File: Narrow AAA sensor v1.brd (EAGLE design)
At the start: 47 x 10.8 mm, 16 parts, among them U1 ATMEGA328P_PDIP

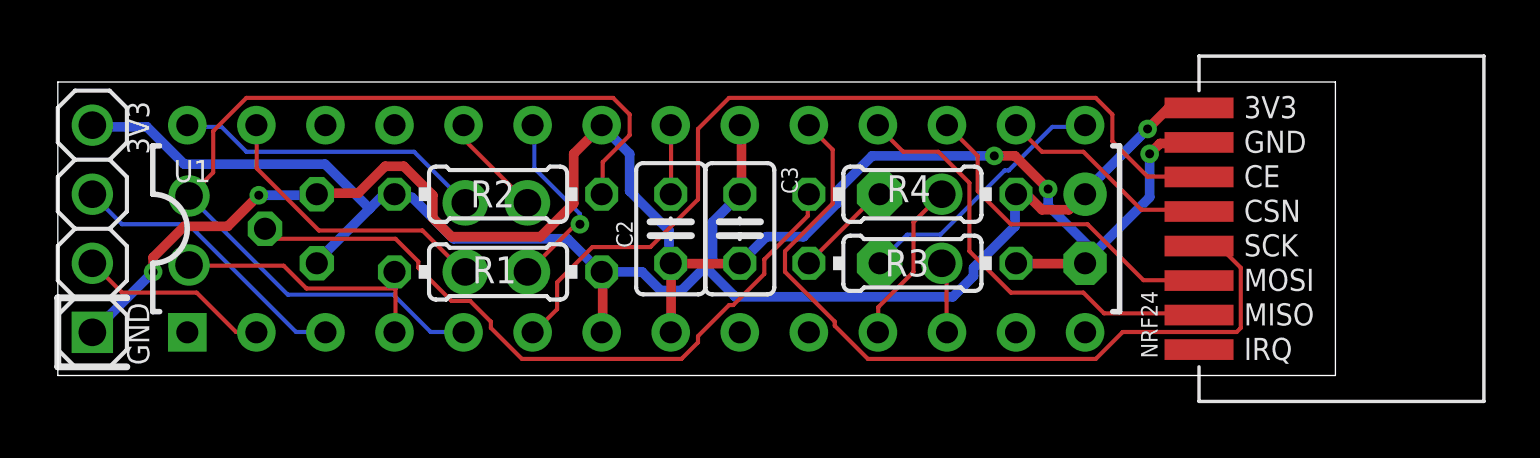
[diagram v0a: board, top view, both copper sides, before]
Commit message: FIXed missing TMP wire
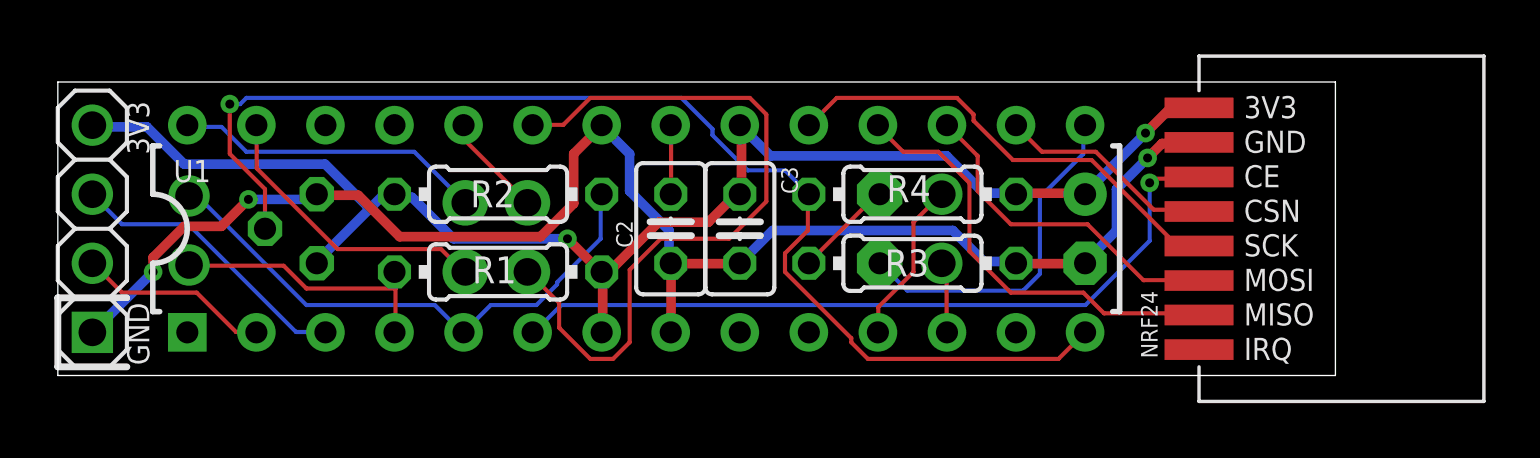
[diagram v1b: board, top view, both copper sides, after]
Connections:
- removed net A2: U1.25
- removed net A3: U1.26
- removed net B0: R4.1, TMP.2
- removed net D7: U1.13
- new net TMP: R4.1, TMP.2, U1.14
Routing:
- net TMP: track 0.00 -> 44.2 mm, vias 0 -> 1
- net B0: track 25.7 -> 0.00 mm
- net A0: track 7.02 -> 27.1 mm, vias 1 -> 0
- net D3: track 34.4 -> 20.3 mm
- net SCK: track 29.2 -> 17.1 mm
- net GND: track 63.9 -> 56.5 mm, vias 5 -> 3
- net VCC: track 59.7 -> 54.6 mm, vias 1 -> 2
- net CE: track 32.0 -> 28.1 mm, vias 0 -> 1
- net B1: track 9.68 -> 12.7 mm
